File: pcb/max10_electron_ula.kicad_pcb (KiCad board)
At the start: 4 copper layers, 50 x 50 mm, 33 parts

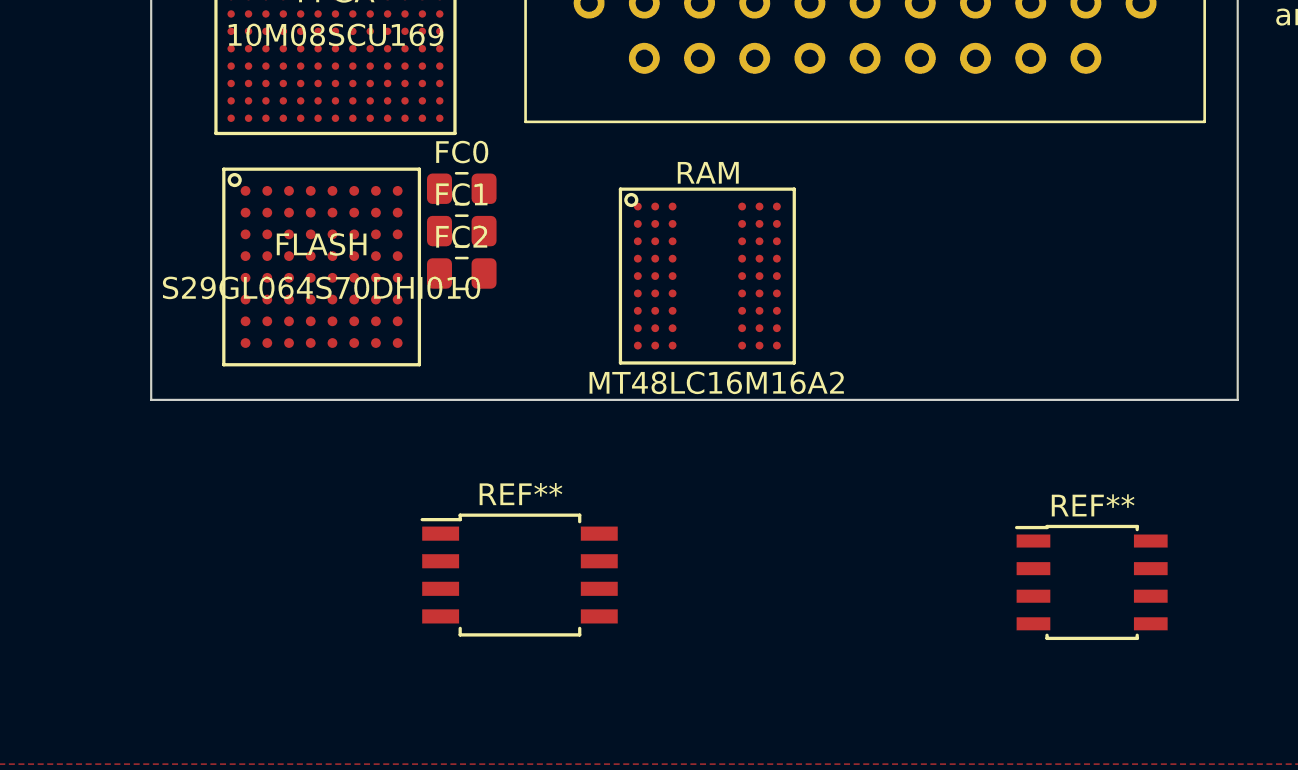
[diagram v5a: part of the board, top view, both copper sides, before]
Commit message: Added serial flash chip
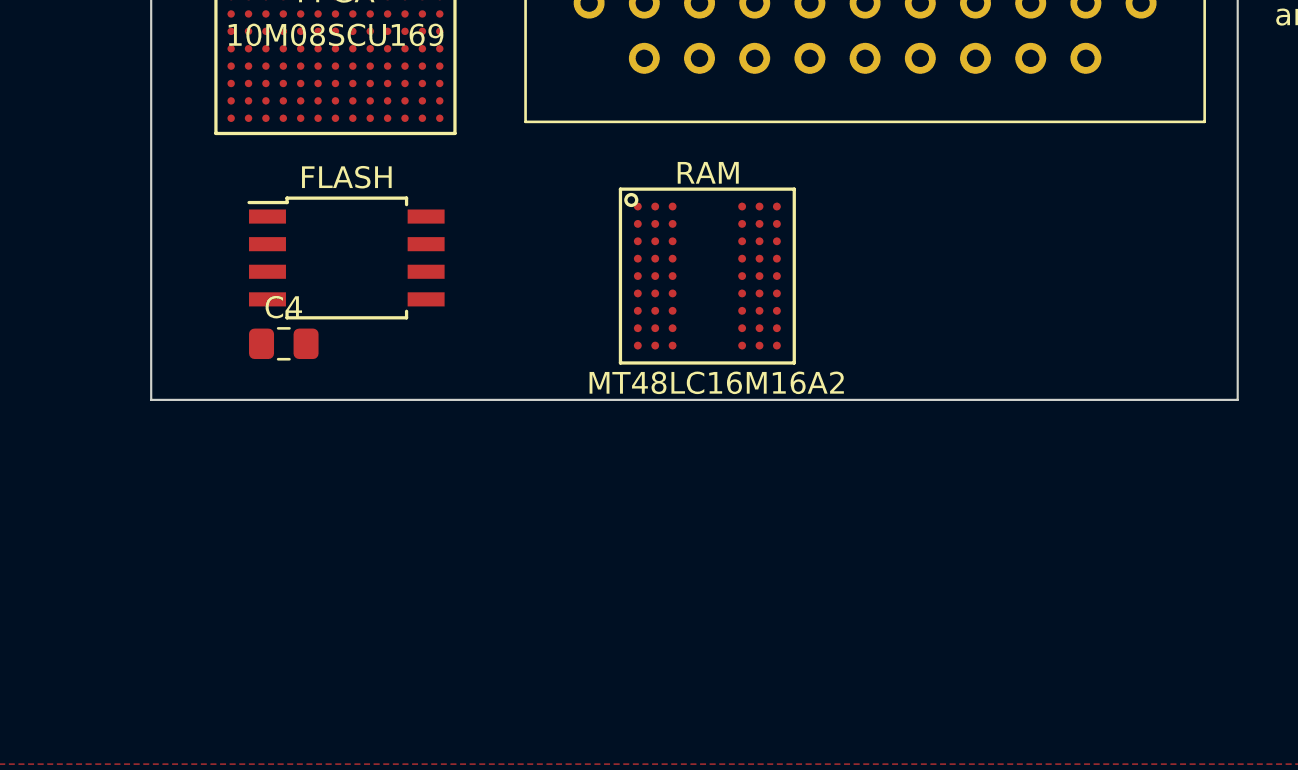
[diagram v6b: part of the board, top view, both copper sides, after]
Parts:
- removed FC0, FC1, FC2: 100n, Capacitor_SMD:C_0805_2012Metric_Pad1.15x1.40mm_HandSolder
- removed the FLASH at (122.8, 88.9)
- removed the REF** at (132.0, 103.1)
- removed the REF** at (158.3, 103.4)
- added C4: 100n, Capacitor_SMD:C_0805_2012Metric_Pad1.15x1.40mm_HandSolder, F.Cu at (121.1, 92.4)
- added FLASH: package TBD, Package_SO:SOIJ-8_5.3x5.3mm_P1.27mm, F.Cu at (124.0, 88.5)

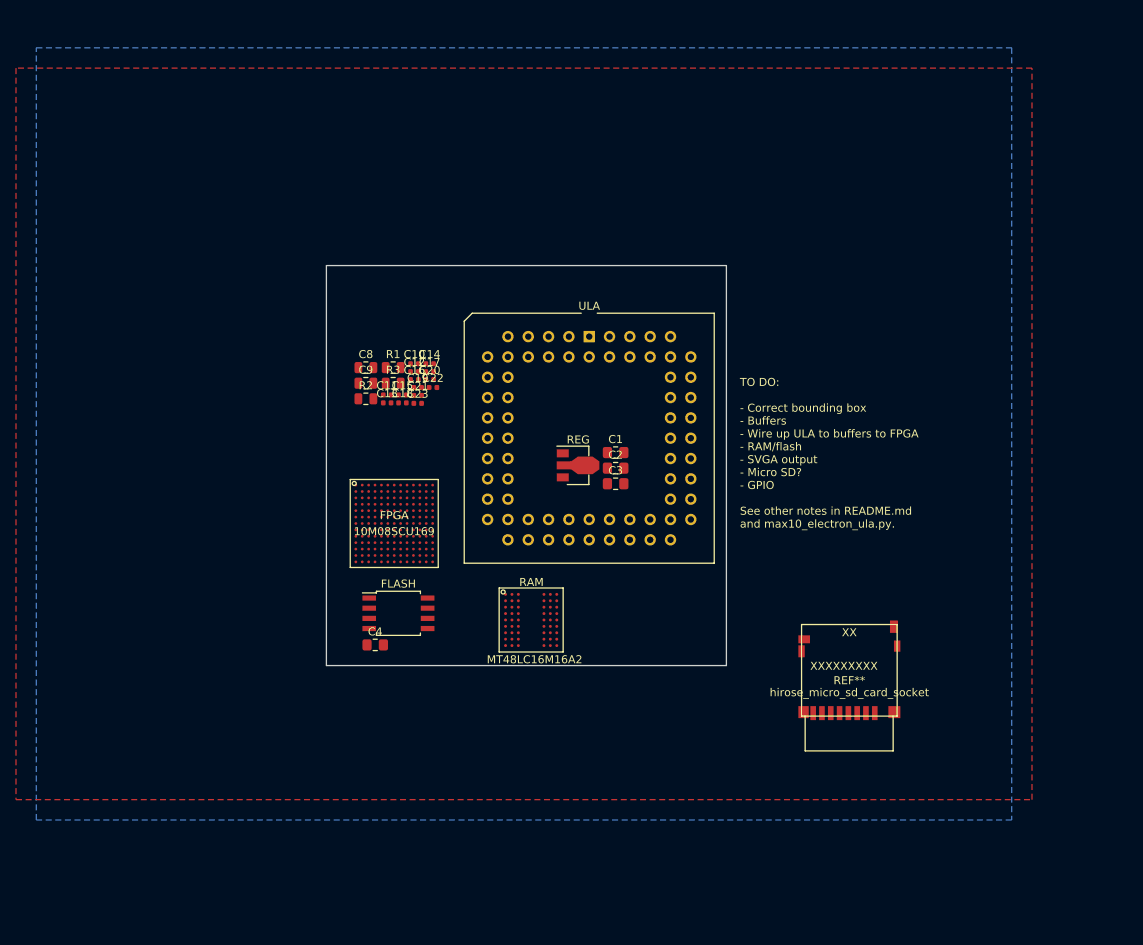
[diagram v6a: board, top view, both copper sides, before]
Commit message: Netlist is getting there -- now all buffers are connected up on the 5V side, and all pullups/decoupling discretes are in there, I think
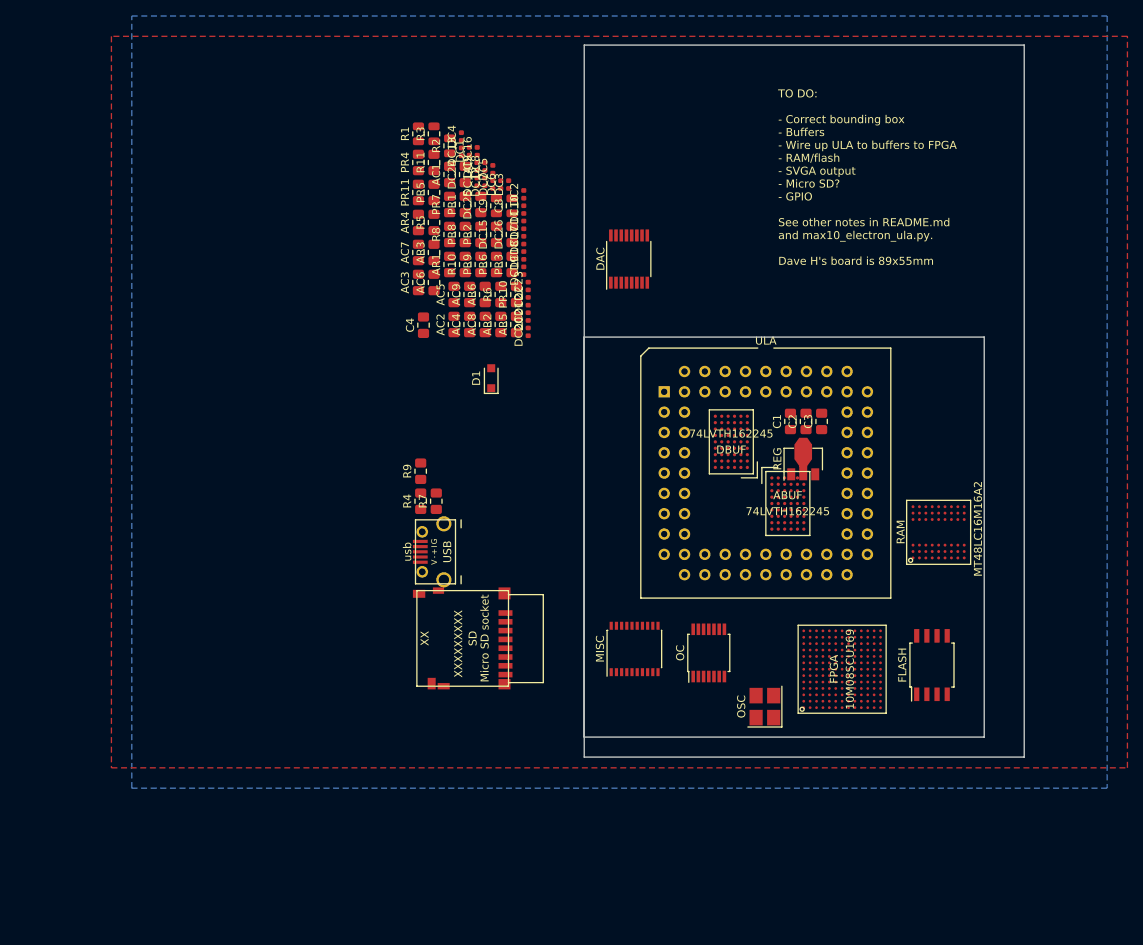
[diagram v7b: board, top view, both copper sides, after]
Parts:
- removed C10, C11, C12, C13, C14, C15, C16, C17, C18, C19, C20, C21, C22, C23: 100n, Capacitor_SMD:C_0402_1005Metric
- removed REF**: hirose_micro_sd_card_socket, myelin-kicad:hirose_micro_sd_card_socket
- removed the ULA at (147.9, 53.9)
- added ABUF: 74LVTH162245, myelin-kicad:ti_zrd_54_pbga, F.Cu at (172.7, 74.7)
- added AC1: 1u, Capacitor_SMD:C_0805_2012Metric_Pad1.15x1.40mm_HandSolder, F.Cu at (130.4, 33.6)
- added AC2: 4.7u, Capacitor_SMD:C_0805_2012Metric_Pad1.15x1.40mm_HandSolder, F.Cu at (131.0, 52.4)
- added AC3: 4.7u, Capacitor_SMD:C_0805_2012Metric_Pad1.15x1.40mm_HandSolder, F.Cu at (126.5, 47.1)
- added AC4: 2.2u, Capacitor_SMD:C_0805_2012Metric_Pad1.15x1.40mm_HandSolder, F.Cu at (132.9, 52.4)
- added AC5: 1u, Capacitor_SMD:C_0805_2012Metric_Pad1.15x1.40mm_HandSolder, F.Cu at (131.0, 48.6)
- added AC6: 2.7n NF, Capacitor_SMD:C_0805_2012Metric_Pad1.15x1.40mm_HandSolder, F.Cu at (128.5, 47.1)
- added AC7: 2.7n NF, Capacitor_SMD:C_0805_2012Metric_Pad1.15x1.40mm_HandSolder, F.Cu at (126.5, 43.4)
- added AC8: 10u, Capacitor_SMD:C_0805_2012Metric_Pad1.15x1.40mm_HandSolder, F.Cu at (134.9, 52.4)
- added AC9: 10u, Capacitor_SMD:C_0805_2012Metric_Pad1.15x1.40mm_HandSolder, F.Cu at (132.9, 48.6)
- added AR1: 560R NF, Resistor_SMD:R_0805_2012Metric_Pad1.15x1.40mm_HandSolder, F.Cu at (130.4, 44.9)
- added AR2: 560R NF, Resistor_SMD:R_0805_2012Metric_Pad1.15x1.40mm_HandSolder, F.Cu at (136.8, 52.4)
- added AR3: NF 10k, Resistor_SMD:R_0805_2012Metric_Pad1.15x1.40mm_HandSolder, F.Cu at (128.5, 43.4)
- added AR4: 10k, Resistor_SMD:R_0805_2012Metric_Pad1.15x1.40mm_HandSolder, F.Cu at (126.5, 39.6)
- added AR5: 10k, Resistor_SMD:R_0805_2012Metric_Pad1.15x1.40mm_HandSolder, F.Cu at (138.8, 52.4)
- added AR6: 10k, Resistor_SMD:R_0805_2012Metric_Pad1.15x1.40mm_HandSolder, F.Cu at (134.9, 48.6)
- added D1: BAT54, Diode_SMD:D_SOD-323_HandSoldering, F.Cu at (135.6, 59.1)
- added DAC: WM8524, Package_SO:TSSOP-16_4.4x5mm_P0.65mm, F.Cu at (152.8, 44.2)
- added DBUF: 74LVTH162245, myelin-kicad:ti_zrd_54_pbga, F.Cu at (165.6, 67.0)
- added DC1: 100n, Capacitor_SMD:C_0402_1005Metric, F.Cu at (132.9, 30.7)
- added DC10: 100n, Capacitor_SMD:C_0402_1005Metric, F.Cu at (139.7, 38.0)
- added DC11: 100n, Capacitor_SMD:C_0402_1005Metric, F.Cu at (139.7, 39.9)
- added DC12: 100n, Capacitor_SMD:C_0402_1005Metric, F.Cu at (134.8, 34.5)
- added DC13: 100n, Capacitor_SMD:C_0402_1005Metric, F.Cu at (131.9, 30.8)
- added DC14: 100n, Capacitor_SMD:C_0402_1005Metric, F.Cu at (133.8, 34.5)
- added DC15: 100n, Capacitor_SMD:C_0805_2012Metric_Pad1.15x1.40mm_HandSolder, F.Cu at (136.3, 41.1)
- added DC16: 100n, Capacitor_SMD:C_0402_1005Metric, F.Cu at (133.9, 30.7)
- added DC17: 100n, Capacitor_SMD:C_0402_1005Metric, F.Cu at (139.7, 41.8)
- added DC18: 100n, Capacitor_SMD:C_0402_1005Metric, F.Cu at (139.7, 43.7)
- added DC19: 100n, Capacitor_SMD:C_0402_1005Metric, F.Cu at (139.7, 45.6)
- added DC2: 100n, Capacitor_SMD:C_0402_1005Metric, F.Cu at (139.7, 36.1)
- added DC20: 100n, Capacitor_SMD:C_0402_1005Metric, F.Cu at (140.2, 53.3)
- added DC21: 100n, Capacitor_SMD:C_0402_1005Metric, F.Cu at (140.2, 51.4)
- added DC22: 100n, Capacitor_SMD:C_0402_1005Metric, F.Cu at (140.2, 49.5)
- added DC23: 100n, Capacitor_SMD:C_0402_1005Metric, F.Cu at (140.2, 47.6)
- added DC24: 100n, Capacitor_SMD:C_0805_2012Metric_Pad1.15x1.40mm_HandSolder, F.Cu at (132.4, 33.6)
- added DC25: 100n, Capacitor_SMD:C_0805_2012Metric_Pad1.15x1.40mm_HandSolder, F.Cu at (134.3, 37.4)
- added DC26: 100n, Capacitor_SMD:C_0805_2012Metric_Pad1.15x1.40mm_HandSolder, F.Cu at (138.2, 41.1)
- added DC3: 100n, Capacitor_SMD:C_0402_1005Metric, F.Cu at (137.8, 34.9)
- added DC4: 100n, Capacitor_SMD:C_0402_1005Metric, F.Cu at (131.9, 28.9)
- added DC5: 100n, Capacitor_SMD:C_0402_1005Metric, F.Cu at (135.8, 33.0)
- added DC6: 100n, Capacitor_SMD:C_0402_1005Metric, F.Cu at (136.8, 34.9)
- added DC7: 100n, Capacitor_SMD:C_0402_1005Metric, F.Cu at (135.8, 34.9)
- added DC8: 100n, Capacitor_SMD:C_0402_1005Metric, F.Cu at (134.8, 32.6)
- added DC9: 100n, Capacitor_SMD:C_0402_1005Metric, F.Cu at (133.8, 32.6)
- added MISC: 74HCT245PW, Package_SO:SSOP-20_4.4x6.5mm_P0.65mm, F.Cu at (153.5, 92.9)
- added OC: 74HCT125PW, Package_SO:TSSOP-14_4.4x5mm_P0.65mm, F.Cu at (162.8, 93.4)
- added OSC: osc, Oscillator:Oscillator_SMD_Abracon_ASE-4Pin_3.2x2.5mm_HandSoldering, F.Cu at (169.8, 100.1)
- added PR1: 10k, Resistor_SMD:R_0805_2012Metric_Pad1.15x1.40mm_HandSolder, F.Cu at (132.4, 37.4)
- added PR10: 10k, Resistor_SMD:R_0805_2012Metric_Pad1.15x1.40mm_HandSolder, F.Cu at (138.8, 48.6)
- added PR11: 10k NF, Resistor_SMD:R_0805_2012Metric_Pad1.15x1.40mm_HandSolder, F.Cu at (126.5, 35.9)
- added PR2: 10k, Resistor_SMD:R_0805_2012Metric_Pad1.15x1.40mm_HandSolder, F.Cu at (134.3, 41.1)
- added PR3: 10k, Resistor_SMD:R_0805_2012Metric_Pad1.15x1.40mm_HandSolder, F.Cu at (138.2, 44.9)
- added PR4: 10k, Resistor_SMD:R_0805_2012Metric_Pad1.15x1.40mm_HandSolder, F.Cu at (126.5, 32.1)
- added PR5: 10k, Resistor_SMD:R_0805_2012Metric_Pad1.15x1.40mm_HandSolder, F.Cu at (128.5, 35.9)
- added PR6: 10k, Resistor_SMD:R_0805_2012Metric_Pad1.15x1.40mm_HandSolder, F.Cu at (136.3, 44.9)
- added PR7: 10k, Resistor_SMD:R_0805_2012Metric_Pad1.15x1.40mm_HandSolder, F.Cu at (130.4, 37.4)
- added PR8: 10k, Resistor_SMD:R_0805_2012Metric_Pad1.15x1.40mm_HandSolder, F.Cu at (132.4, 41.1)
- added PR9: 10k, Resistor_SMD:R_0805_2012Metric_Pad1.15x1.40mm_HandSolder, F.Cu at (134.3, 44.9)
- added R10: 68R, Resistor_SMD:R_0805_2012Metric_Pad1.15x1.40mm_HandSolder, F.Cu at (132.4, 44.9)
- added R11: 1k5, Resistor_SMD:R_0805_2012Metric_Pad1.15x1.40mm_HandSolder, F.Cu at (128.5, 32.1)
- added R4: 10k, Resistor_SMD:R_0805_2012Metric_Pad1.15x1.40mm_HandSolder, F.Cu at (126.8, 74.5)
- added R5: 100R, Resistor_SMD:R_0805_2012Metric_Pad1.15x1.40mm_HandSolder, F.Cu at (128.5, 39.6)
- added R6: 1k, Resistor_SMD:R_0805_2012Metric_Pad1.15x1.40mm_HandSolder, F.Cu at (136.8, 48.6)
- added R7: 1k, Resistor_SMD:R_0805_2012Metric_Pad1.15x1.40mm_HandSolder, F.Cu at (128.7, 74.5)
- added R8: 1k, Resistor_SMD:R_0805_2012Metric_Pad1.15x1.40mm_HandSolder, F.Cu at (130.4, 41.1)
- added R9: 68R, Resistor_SMD:R_0805_2012Metric_Pad1.15x1.40mm_HandSolder, F.Cu at (126.8, 70.7)
- added SD: Micro SD socket, myelin-kicad:hirose_micro_sd_card_socket, F.Cu at (126.3, 91.6)
- added ULA: ULA header, modified-kicad:PLCC-68_THT-Socket-Electron-ULA, F.Cu at (169.9, 58.2)
- added USB: usb, myelin-kicad:micro_usb_b_smd_molex, F.Cu at (129.1, 80.8)
- C4: value 100n -> 2.7n
- moved FLASH 67.0 mm to (190.7, 94.9), turned to 90 degrees
- moved FPGA 58.9 mm to (179.5, 95.5), turned to 90 degrees
- moved RAM 52.1 mm to (191.5, 78.3), turned to 90 degrees
- moved C4 40.4 mm to (127.1, 52.5), turned to 90 degrees
- moved R2 33.3 mm to (130.4, 30.0), turned to 90 degrees
- moved R3 31.6 mm to (128.5, 28.5), turned to 90 degrees
- moved R1 29.4 mm to (126.5, 28.5), turned to 90 degrees
- moved REG 28.6 mm to (174.6, 69.6), turned to 90 degrees
- moved C9 27.5 mm to (136.3, 37.5), turned to 90 degrees
- moved C8 27.2 mm to (138.2, 37.5), turned to 90 degrees
- moved C3 26.9 mm to (176.9, 64.5), turned to 90 degrees
- moved C2 24.5 mm to (175.0, 64.5), turned to 90 degrees
- moved C1 22.2 mm to (173.0, 64.5), turned to 90 degrees
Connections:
- C4 pad 1: 3V3 -> PHI_OUT_5V
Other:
- board size 50 x 50 mm -> 55 x 89 mm
- board text added: "TO DO: - Correct bounding box - Buffers - Wire up ULA to buffers to FPGA - RAM/flash - SVGA output - Micro SD? - GPIO See other notes in README.md and max10_electron_ula.py. Dave H's board is 89x55mm"
- board text removed: "TO DO: - Correct bounding box - Buffers - Wire up ULA to buffers to FPGA - RAM/flash - SVGA output - Micro SD? - GPIO See other notes in README.md and max10_electron_ula.py."
